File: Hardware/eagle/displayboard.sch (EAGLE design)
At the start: 15 parts, among them IC1 24C16, J1 CON_HEADER_1X08-SMD, J2 FH12-10S-0.5SH, J3 CON_HEADER_1X08-SMD

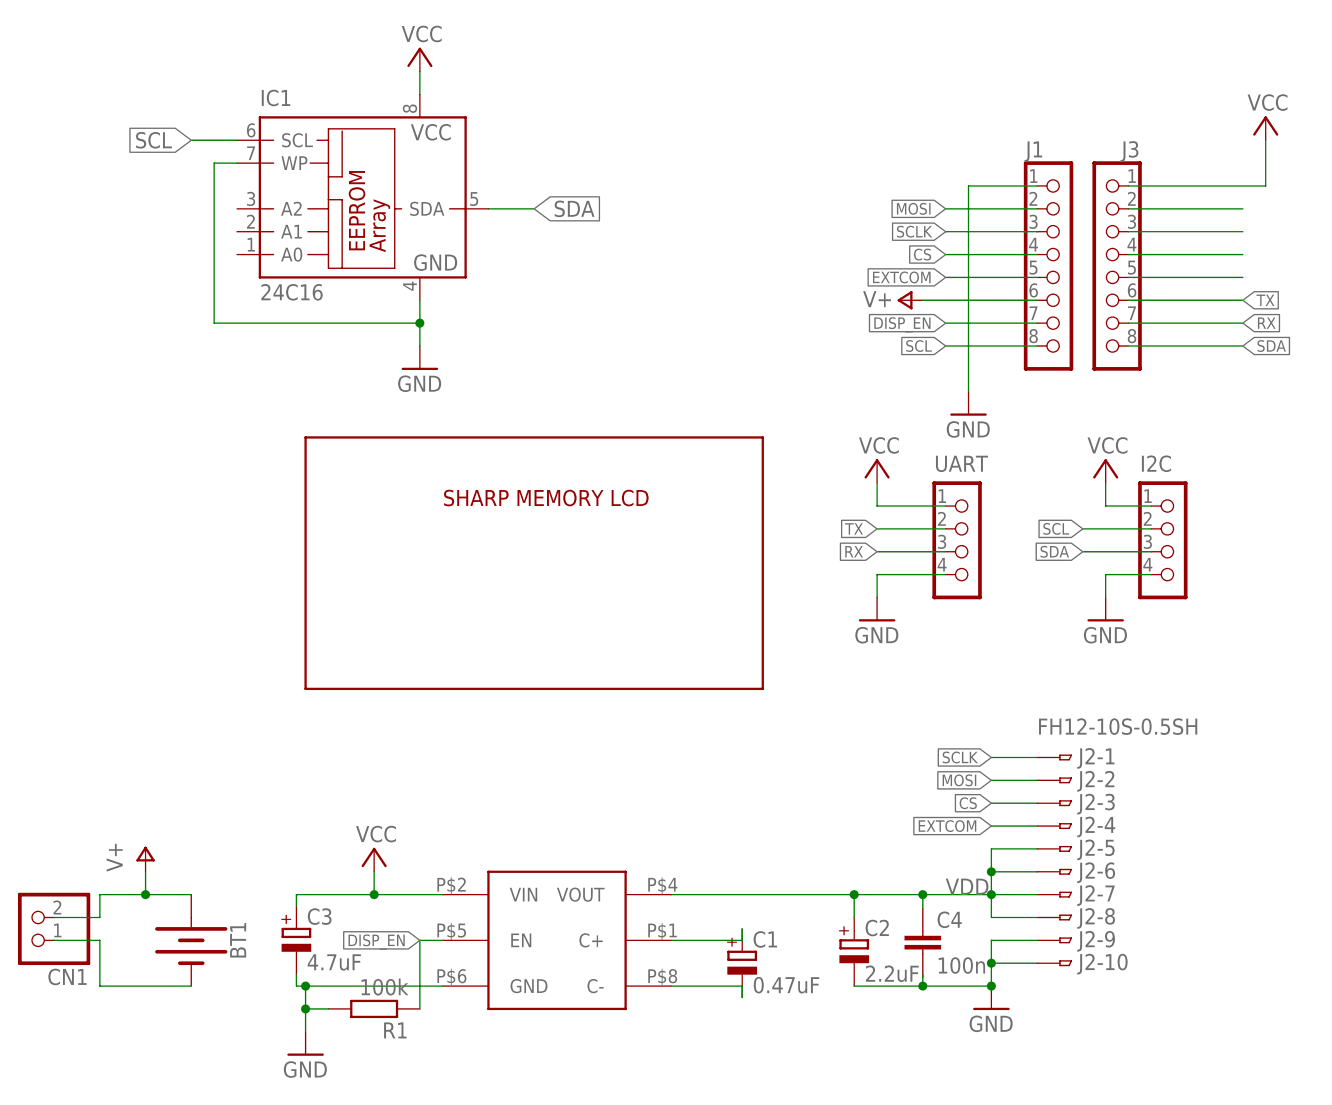
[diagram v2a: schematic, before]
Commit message: Spin a fixed board revision
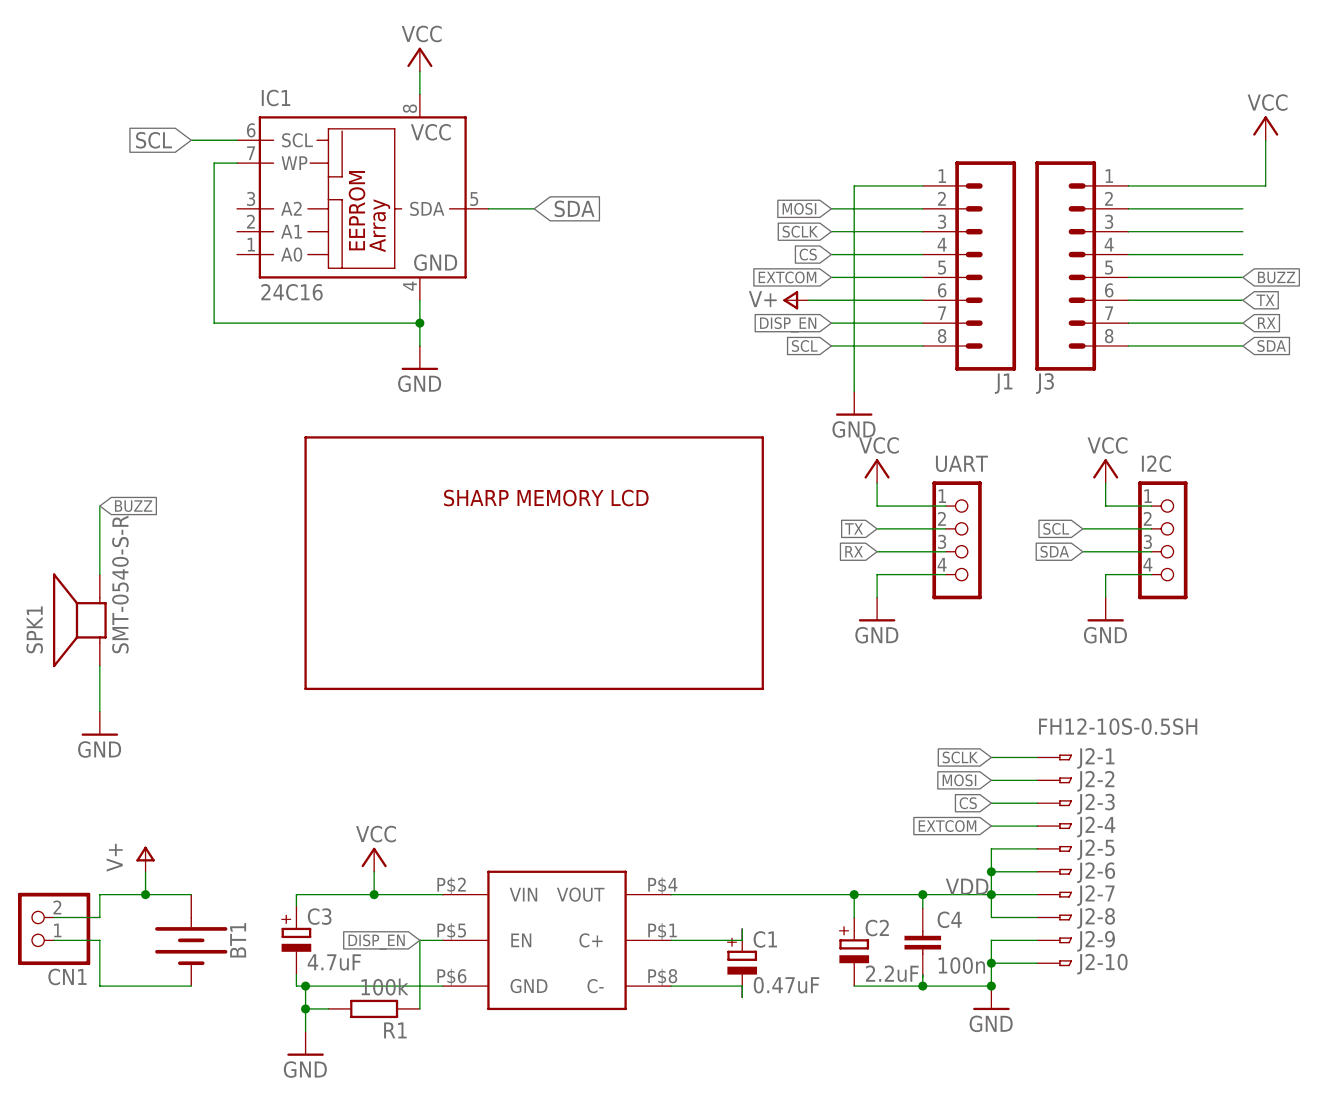
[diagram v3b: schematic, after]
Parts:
- added SPK1: SMT-0540-S-R, adafruit:SMT-0540-S-R
- J1, J3: value CON_HEADER_1X08-SMD -> (none); device dp_devices.v6:CON_HEADER_1X08-SMD -> SparkFun-Connectors:CONN_08SMD-COMBO-FEMALE
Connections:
- removed net N$11: J3.5
- new net BUZZ: J3.5, SPK1.-
- net GND: now also SPK1.+
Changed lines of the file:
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@@
 <layer number="112" name="tSilk" color="7" fill="1" visible="yes" active="yes"/>
 <layer number="113" name="IDFDebug" color="4" fill="1" visible="yes" active="yes"/>
+<layer number="114" name="Badge_Outline" color="7" fill="1" visible="yes" active="yes"/>
+<layer number="115" name="ReferenceISLANDS" color="7" fill="1" visible="yes" active="yes"/>
 <layer number="116" name="Patch_BOT" color="9" fill="4" visible="yes" active="yes"/>
 <layer number="118" name="Rect_Pads" color="7" fill="1" visible="yes" active="yes"/>
@@
 <part name="C4" library="rcl" library_urn="urn:adsk.eagle:library:334" deviceset="C-EU" device="C1206K" value="100n"/>
 <part name="U$2" library="SparkFun-Electromechanical" deviceset="MEMORYLCD" device=""/>
-<part name="J1" library="dp_devices.v6" deviceset="CON_HEADER_1X08" device="-SMD"/>
-<part name="J3" library="dp_devices.v6" deviceset="CON_HEADER_1X08" device="-SMD"/>
 <part name="P+1" library="supply1" library_urn="urn:adsk.eagle:library:371" deviceset="VCC" device=""/>
 <part name="CN1" library="pinhead" library_urn="urn:adsk.eagle:library:325" deviceset="PINHD-1X2" device=""/>
@@
 <part name="GND6" library="supply1" library_urn="urn:adsk.eagle:library:371" deviceset="GND" device=""/>
 <part name="P+7" library="supply1" library_urn="urn:adsk.eagle:library:371" deviceset="VCC" device=""/>
+<part name="J1" library="SparkFun-Connectors" deviceset="CONN_08" device="SMD-COMBO-FEMALE"/>
+<part name="J3" library="SparkFun-Connectors" deviceset="CONN_08" device="SMD-COMBO-FEMALE"/>
+<part name="SPK1" library="adafruit" library_urn="urn:adsk.eagle:library:420" deviceset="SMT-0540-S-R" device=""/>
+<part name="GND7" library="supply1" library_urn="urn:adsk.eagle:library:371" deviceset="GND" device=""/>
 </parts>
 <sheets>
@@
 <instance part="J2" gate="-9" x="236.22" y="73.66"/>
 <instance part="J2" gate="-10" x="236.22" y="71.12"/>
-<instance part="GND1" gate="1" x="226.06" y="132.08"/>
+<instance part="GND1" gate="1" x="213.36" y="132.08"/>
 <instance part="P+2" gate="VCC" x="259.08" y="165.1" smashed="yes">
 <attribute name="VALUE" x="261.62" y="167.64" size="1.778" layer="96" rot="R180"/>
@@
 <instance part="C4" gate="G$1" x="220.98" y="74.676"/>
 <instance part="U$2" gate="G$1" x="177.8" y="116.84"/>
-<instance part="J1" gate="J" x="233.68" y="149.86"/>
-<instance part="J3" gate="J" x="243.84" y="149.86" rot="MR0"/>
 <instance part="P+1" gate="VCC" x="160.02" y="83.82" smashed="yes">
 <attribute name="VALUE" x="162.56" y="86.36" size="1.778" layer="96" rot="R180"/>
 </instance>
 <instance part="CN1" gate="G$1" x="121.92" y="76.2" rot="R180"/>
-<instance part="P+3" gate="1" x="218.44" y="144.78" smashed="yes" rot="R90">
-<attribute name="VALUE" x="217.678" y="145.796" size="1.778" layer="96" rot="R180"/>
+<instance part="P+3" gate="1" x="205.74" y="144.78" smashed="yes" rot="R90">
+<attribute name="VALUE" x="204.978" y="145.796" size="1.778" layer="96" rot="R180"/>
 </instance>
 <instance part="P+4" gate="1" x="134.62" y="83.82"/>
@@
 <attribute name="VALUE" x="167.64" y="175.26" size="1.778" layer="96" rot="R180"/>
 </instance>
+<instance part="J1" gate="G$1" x="226.06" y="149.86" rot="R180"/>
+<instance part="J3" gate="G$1" x="238.76" y="149.86" rot="MR180"/>
+<instance part="SPK1" gate="G$1" x="129.54" y="109.22" rot="R90"/>
+<instance part="GND7" gate="1" x="129.54" y="96.52"/>
 </instances>
 <busses>
@@
 <net name="SCL" class="0">
 <segment>
-<wire x1="233.68" y1="139.7" x2="223.52" y2="139.7" width="0.1524" layer="91"/>
-<pinref part="J1" gate="J" pin="8"/>
-<label x="223.52" y="139.7" size="1.27" layer="95" rot="R180" xref="yes"/>
+<wire x1="220.98" y1="139.7" x2="210.82" y2="139.7" width="0.1524" layer="91"/>
+<label x="210.82" y="139.7" size="1.27" layer="95" rot="R180" xref="yes"/>
+<pinref part="J1" gate="G$1" pin="8"/>
 </segment>
 <segment>
@@
 </segment>
 <segment>
-<wire x1="233.68" y1="147.32" x2="223.52" y2="147.32" width="0.1524" layer="91"/>
-<label x="223.52" y="147.32" size="1.27" layer="95" rot="R180" xref="yes"/>
-<pinref part="J1" gate="J" pin="5"/>
+<wire x1="220.98" y1="147.32" x2="210.82" y2="147.32" width="0.1524" layer="91"/>
+<label x="210.82" y="147.32" size="1.27" layer="95" rot="R180" xref="yes"/>
+<pinref part="J1" gate="G$1" pin="5"/>
 </segment>
 </net>
@@
 </segment>
 <segment>
-<wire x1="233.68" y1="149.86" x2="223.52" y2="149.86" width="0.1524" layer="91"/>
-<label x="223.52" y="149.86" size="1.27" layer="95" rot="R180" xref="yes"/>
-<pinref part="J1" gate="J" pin="4"/>
+<wire x1="220.98" y1="149.86" x2="210.82" y2="149.86" width="0.1524" layer="91"/>
+<label x="210.82" y="149.86" size="1.27" layer="95" rot="R180" xref="yes"/>
+<pinref part="J1" gate="G$1" pin="4"/>
 </segment>
 </net>
@@
 </segment>
 <segment>
-<wire x1="233.68" y1="154.94" x2="223.52" y2="154.94" width="0.1524" layer="91"/>
-<label x="223.52" y="154.94" size="1.27" layer="95" rot="R180" xref="yes"/>
-<pinref part="J1" gate="J" pin="2"/>
+<wire x1="220.98" y1="154.94" x2="210.82" y2="154.94" width="0.1524" layer="91"/>
+<label x="210.82" y="154.94" size="1.27" layer="95" rot="R180" xref="yes"/>
+<pinref part="J1" gate="G$1" pin="2"/>
 </segment>
 </net>
@@
 </segment>
 <segment>
-<wire x1="233.68" y1="152.4" x2="223.52" y2="152.4" width="0.1524" layer="91"/>
-<label x="223.52" y="152.4" size="1.27" layer="95" rot="R180" xref="yes"/>
-<pinref part="J1" gate="J" pin="3"/>
+<wire x1="220.98" y1="152.4" x2="210.82" y2="152.4" width="0.1524" layer="91"/>
+<label x="210.82" y="152.4" size="1.27" layer="95" rot="R180" xref="yes"/>
+<pinref part="J1" gate="G$1" pin="3"/>
 </segment>
 </net>
 <net name="GND" class="0">
 <segment>
-<wire x1="233.68" y1="157.48" x2="226.06" y2="157.48" width="0.1524" layer="91"/>
+<wire x1="220.98" y1="157.48" x2="213.36" y2="157.48" width="0.1524" layer="91"/>
 <pinref part="GND1" gate="1" pin="GND"/>
-<wire x1="226.06" y1="134.62" x2="226.06" y2="157.48" width="0.1524" layer="91"/>
-<pinref part="J1" gate="J" pin="1"/>
+<wire x1="213.36" y1="134.62" x2="213.36" y2="157.48" width="0.1524" layer="91"/>
+<pinref part="J1" gate="G$1" pin="1"/>
 </segment>
 <segment>
@@
 <junction x="165.1" y="142.24"/>
 </segment>
+<segment>
+<pinref part="SPK1" gate="G$1" pin="+"/>
+<wire x1="129.54" y1="104.14" x2="129.54" y2="99.06" width="0.1524" layer="91"/>
+<pinref part="GND7" gate="1" pin="GND"/>
+</segment>
 </net>
 <net name="VCC" class="0">
@@
 <wire x1="243.84" y1="157.48" x2="259.08" y2="157.48" width="0.1524" layer="91"/>
 <wire x1="259.08" y1="157.48" x2="259.08" y2="162.56" width="0.1524" layer="91"/>
-<pinref part="J3" gate="J" pin="1"/>
+<pinref part="J3" gate="G$1" pin="1"/>
 </segment>
 <segment>
@@
 <segment>
 <wire x1="243.84" y1="154.94" x2="256.54" y2="154.94" width="0.1524" layer="91"/>
-<pinref part="J3" gate="J" pin="2"/>
+<pinref part="J3" gate="G$1" pin="2"/>
 </segment>
 </net>
@@
 <segment>
 <wire x1="243.84" y1="152.4" x2="256.54" y2="152.4" width="0.1524" layer="91"/>
-<pinref part="J3" gate="J" pin="3"/>
+<pinref part="J3" gate="G$1" pin="3"/>
 </segment>
 </net>
@@
 <segment>
 <wire x1="243.84" y1="149.86" x2="256.54" y2="149.86" width="0.1524" layer="91"/>
-<pinref part="J3" gate="J" pin="4"/>
-</segment>
-</net>
-<net name="N$11" class="0">
+<pinref part="J3" gate="G$1" pin="4"/>
+</segment>
+</net>
+<net name="BUZZ" class="0">
 <segment>
 <wire x1="243.84" y1="147.32" x2="256.54" y2="147.32" width="0.1524" layer="91"/>
-<pinref part="J3" gate="J" pin="5"/>
+<pinref part="J3" gate="G$1" pin="5"/>
+<label x="256.54" y="147.32" size="1.27" layer="95" xref="yes"/>
+</segment>
+<segment>
+<pinref part="SPK1" gate="G$1" pin="-"/>
+<wire x1="129.54" y1="114.3" x2="129.54" y2="121.92" width="0.1524" layer="91"/>
+<label x="129.54" y="121.92" size="1.27" layer="95" xref="yes"/>
 </segment>
 </net>
@@
 <segment>
 <wire x1="243.84" y1="144.78" x2="256.54" y2="144.78" width="0.1524" layer="91"/>
-<pinref part="J3" gate="J" pin="6"/>
 <label x="256.54" y="144.78" size="1.27" layer="95" xref="yes"/>
+<pinref part="J3" gate="G$1" pin="6"/>
 </segment>
 <segment>
@@
 <segment>
 <wire x1="243.84" y1="142.24" x2="256.54" y2="142.24" width="0.1524" layer="91"/>
-<pinref part="J3" gate="J" pin="7"/>
 <label x="256.54" y="142.24" size="1.27" layer="95" xref="yes"/>
+<pinref part="J3" gate="G$1" pin="7"/>
 </segment>
 <segment>
@@
 <segment>
 <wire x1="243.84" y1="139.7" x2="256.54" y2="139.7" width="0.1524" layer="91"/>
-<pinref part="J3" gate="J" pin="8"/>
 <label x="256.54" y="139.7" size="1.27" layer="95" xref="yes"/>
+<pinref part="J3" gate="G$1" pin="8"/>
 </segment>
 <segment>
@@
 </segment>
 <segment>
-<wire x1="233.68" y1="142.24" x2="223.52" y2="142.24" width="0.1524" layer="91"/>
-<label x="223.52" y="142.24" size="1.27" layer="95" rot="R180" xref="yes"/>
-<pinref part="J1" gate="J" pin="7"/>
+<wire x1="220.98" y1="142.24" x2="210.82" y2="142.24" width="0.1524" layer="91"/>
+<label x="210.82" y="142.24" size="1.27" layer="95" rot="R180" xref="yes"/>
+<pinref part="J1" gate="G$1" pin="7"/>
 </segment>
 </net>
@@
 </segment>
 <segment>
-<pinref part="J1" gate="J" pin="6"/>
-<wire x1="233.68" y1="144.78" x2="220.98" y2="144.78" width="0.1524" layer="91"/>
+<wire x1="220.98" y1="144.78" x2="208.28" y2="144.78" width="0.1524" layer="91"/>
 <pinref part="P+3" gate="1" pin="V+"/>
-</segment>
-</net>
+<pinref part="J1" gate="G$1" pin="6"/>
+</segment>
+</net>
